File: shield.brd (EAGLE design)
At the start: 160 x 100 mm, 12 parts

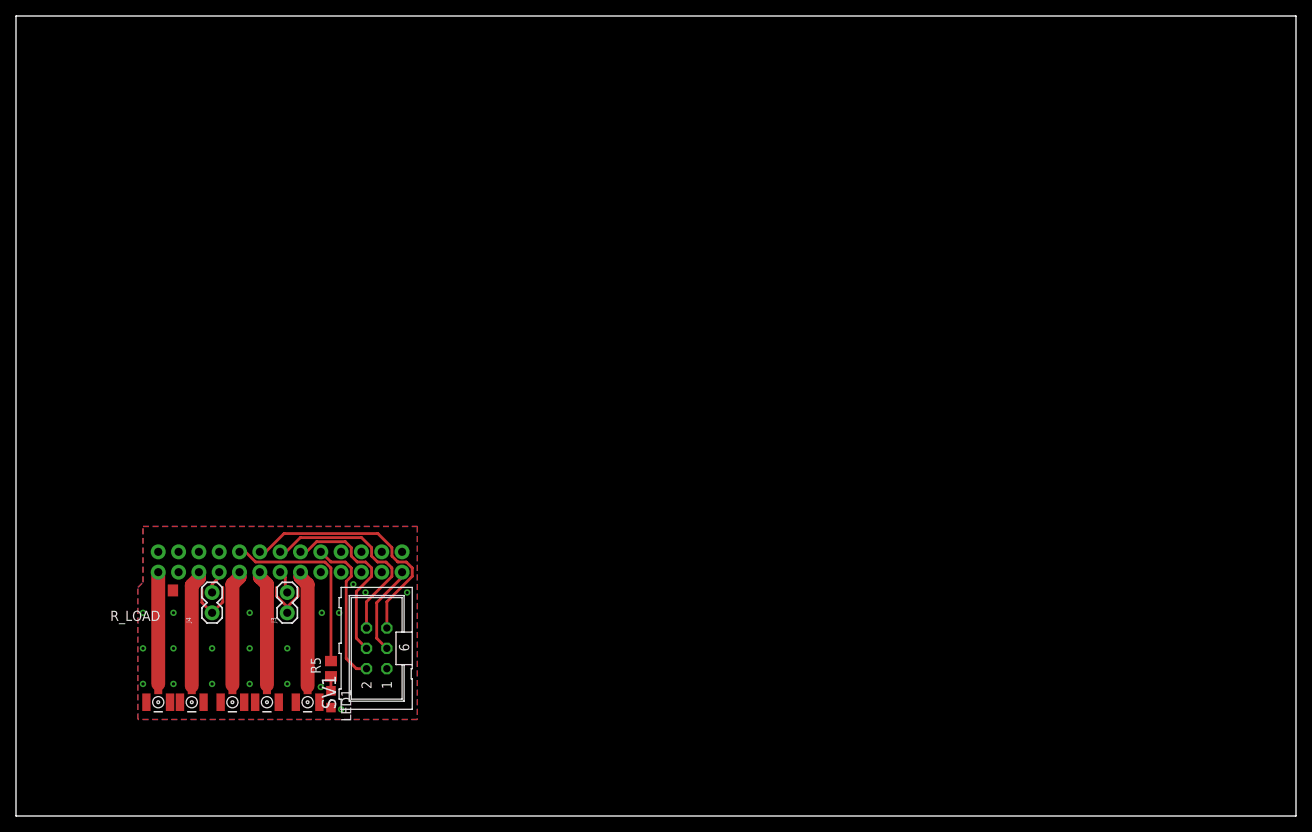
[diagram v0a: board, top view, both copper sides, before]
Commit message: Dimension, moved components to ensure enough distance from main header
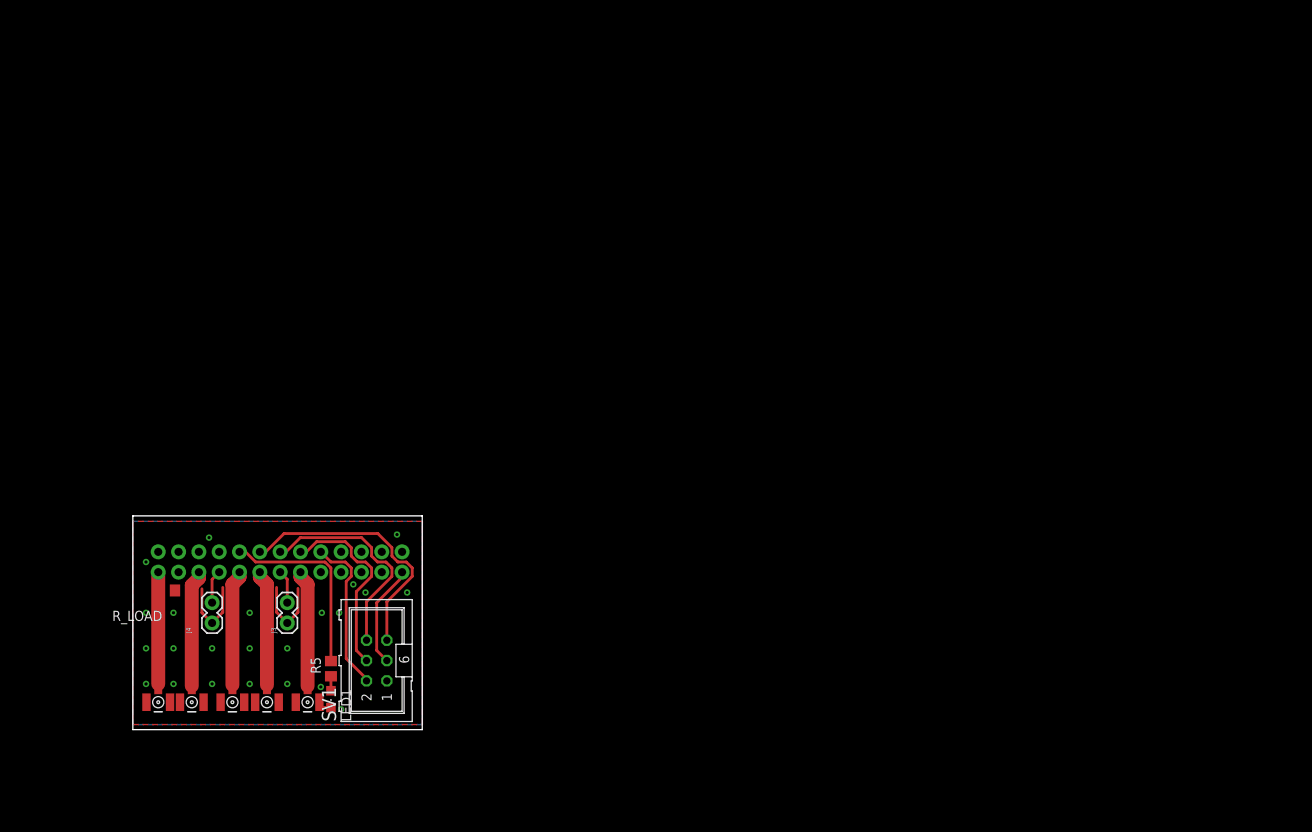
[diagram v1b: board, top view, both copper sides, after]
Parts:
- moved SV1 1.52 mm to (45.1, 19.4)
- moved J3 1.27 mm to (33.9, 24.1)
- moved J4 1.27 mm to (24.5, 24.1)
- moved R_LOAD 0.25 mm to (18.9, 28.2)
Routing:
- net GND: track 24.6 -> 33.2 mm, vias 20 -> 23
- net N$11: track 25.7 -> 27.2 mm
- net N$12: track 31.2 -> 32.7 mm
- net N$10: track 22.8 -> 24.3 mm
- net N$8: track 2.91 -> 4.18 mm
- net N$7: track 2.91 -> 4.18 mm
- net N$9: track 19.3 -> 20.1 mm
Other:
- board size 160 x 100 mm -> 36.2 x 26.7 mm

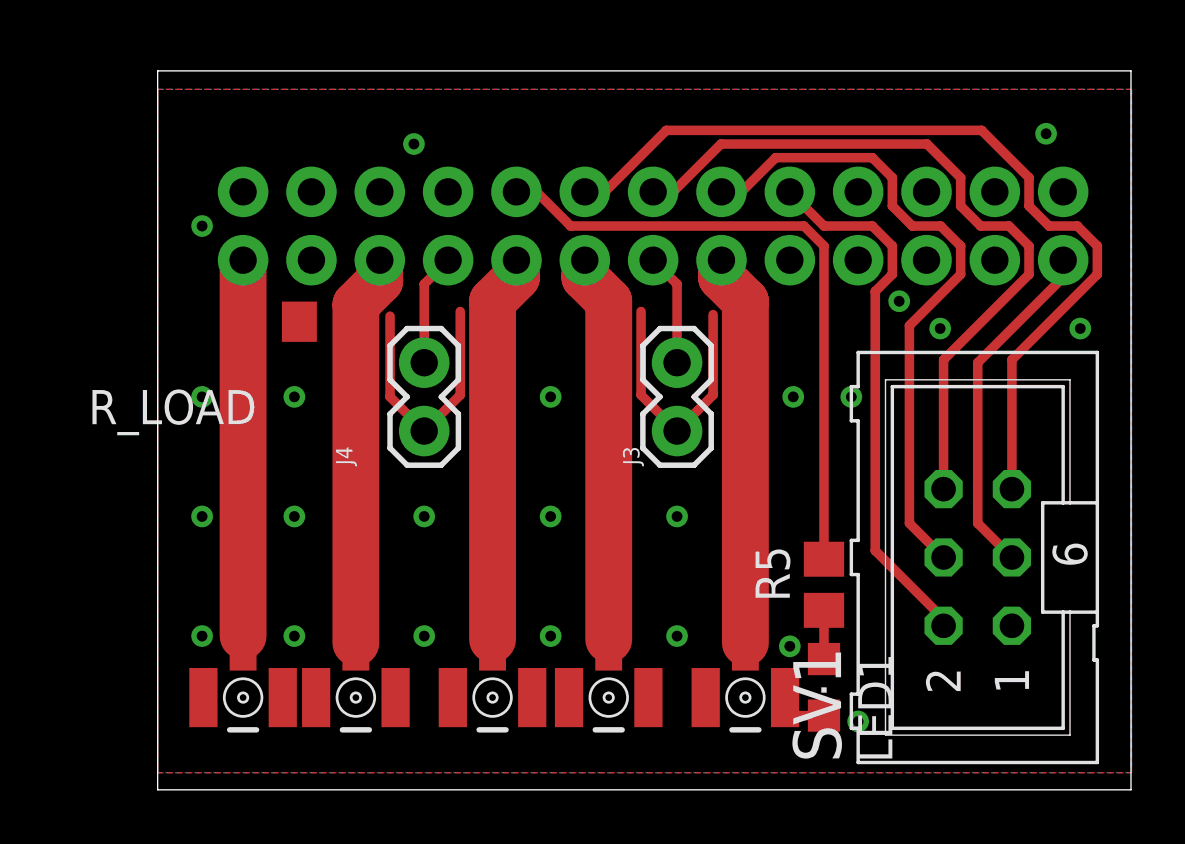
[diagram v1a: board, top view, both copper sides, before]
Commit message: Mirrored design to match header on FPGA
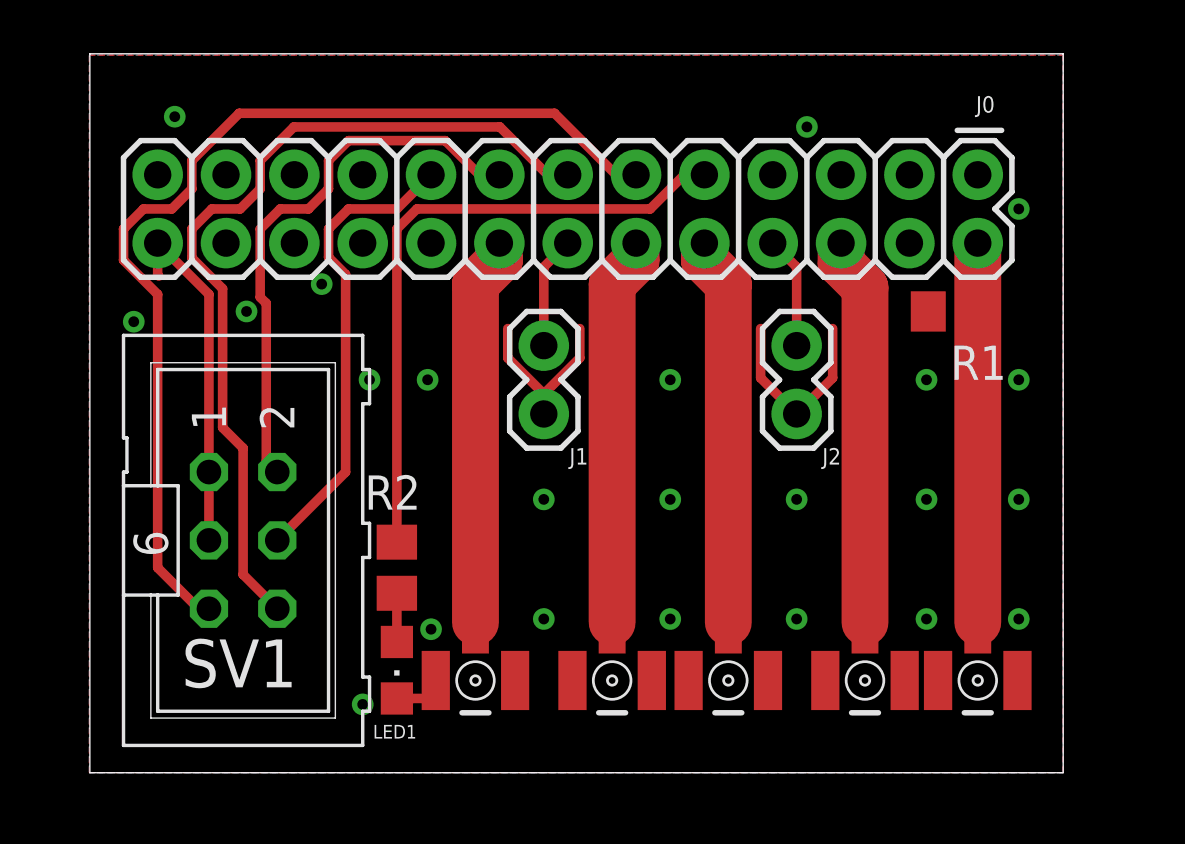
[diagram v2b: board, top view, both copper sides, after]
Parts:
- removed J3, J4: (no value), SparkFun-Connectors:1X02
- removed R5: (no value), rcl:R0805
- removed R_LOAD: 200, rcl:R0805
- added J0: (no value), SparkFun-Connectors:2X13
- added J1: (no value), SparkFun-Connectors:1X02
- added R1: 200, rcl:R0805
- added R2: (no value), rcl:R0805
- J2: device SparkFun-Connectors:2X13 -> SparkFun-Connectors:1X02
- moved SV1 27.3 mm to (17.8, 20.1), turned to 270 degrees
- moved X_S 27.3 mm to (45.1, 14.9)
- moved J2 22.2 mm to (38.4, 24.8), flipped to the top, turned to 90 degrees
- moved X_M1 18.9 mm to (40.9, 14.9)
- moved LED1 15.9 mm to (23.5, 15.2)
- moved X_M4 10.1 mm to (26.4, 14.9)
- moved X_M2 8.79 mm to (35.8, 14.9)
- moved X_M3 0.65 mm to (31.5, 14.9)
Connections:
- net GND: now also J0.26, J1.1, J2.1, R1.1; no longer J2.26, J3.1, J4.1, R_LOAD.1
- net N$1: now also J0.2, R1.2; no longer J2.2, R_LOAD.2
- net N$10: now also J0.15, SV1.2; no longer J2.15, SV1.4
- net N$11: now also J0.13; no longer J2.13
- net N$12: now also J0.11; no longer J2.11
- net N$19: now also R2.1; no longer R5.1
- net N$2: now also J0.6; no longer J2.6
- net N$20: now also J0.9, R2.2; no longer J2.9, R5.2
- net N$3: now also J0.3; no longer J2.3
- net N$4: now also J0.16; no longer J2.16
- net N$5: now also J0.10; no longer J2.10
- net N$6: now also J0.12; no longer J2.12
- net N$7: now also J0.8, J2.2; no longer J2.8, J4.2
- net N$8: now also J0.14, J1.2; no longer J2.14, J3.2
- net N$9: now also J0.17, SV1.4; no longer J2.17, SV1.2
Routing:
- net N$12: track 32.7 -> 38.0 mm
- net N$11: track 27.2 -> 32.3 mm
- net GND: track 33.2 -> 28.9 mm
- net N$10: track 24.3 -> 20.7 mm
- net N$9: track 20.1 -> 17.5 mm
- net N$1: track 14.0 -> 14.7 mm
- net N$5: track 14.5 -> 15.1 mm
- net N$6: track 14.5 -> 15.1 mm
- net N$4: track 14.6 -> 15.1 mm
- net N$2: track 14.6 -> 15.1 mm
